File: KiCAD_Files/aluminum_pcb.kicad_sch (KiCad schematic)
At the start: 29 parts

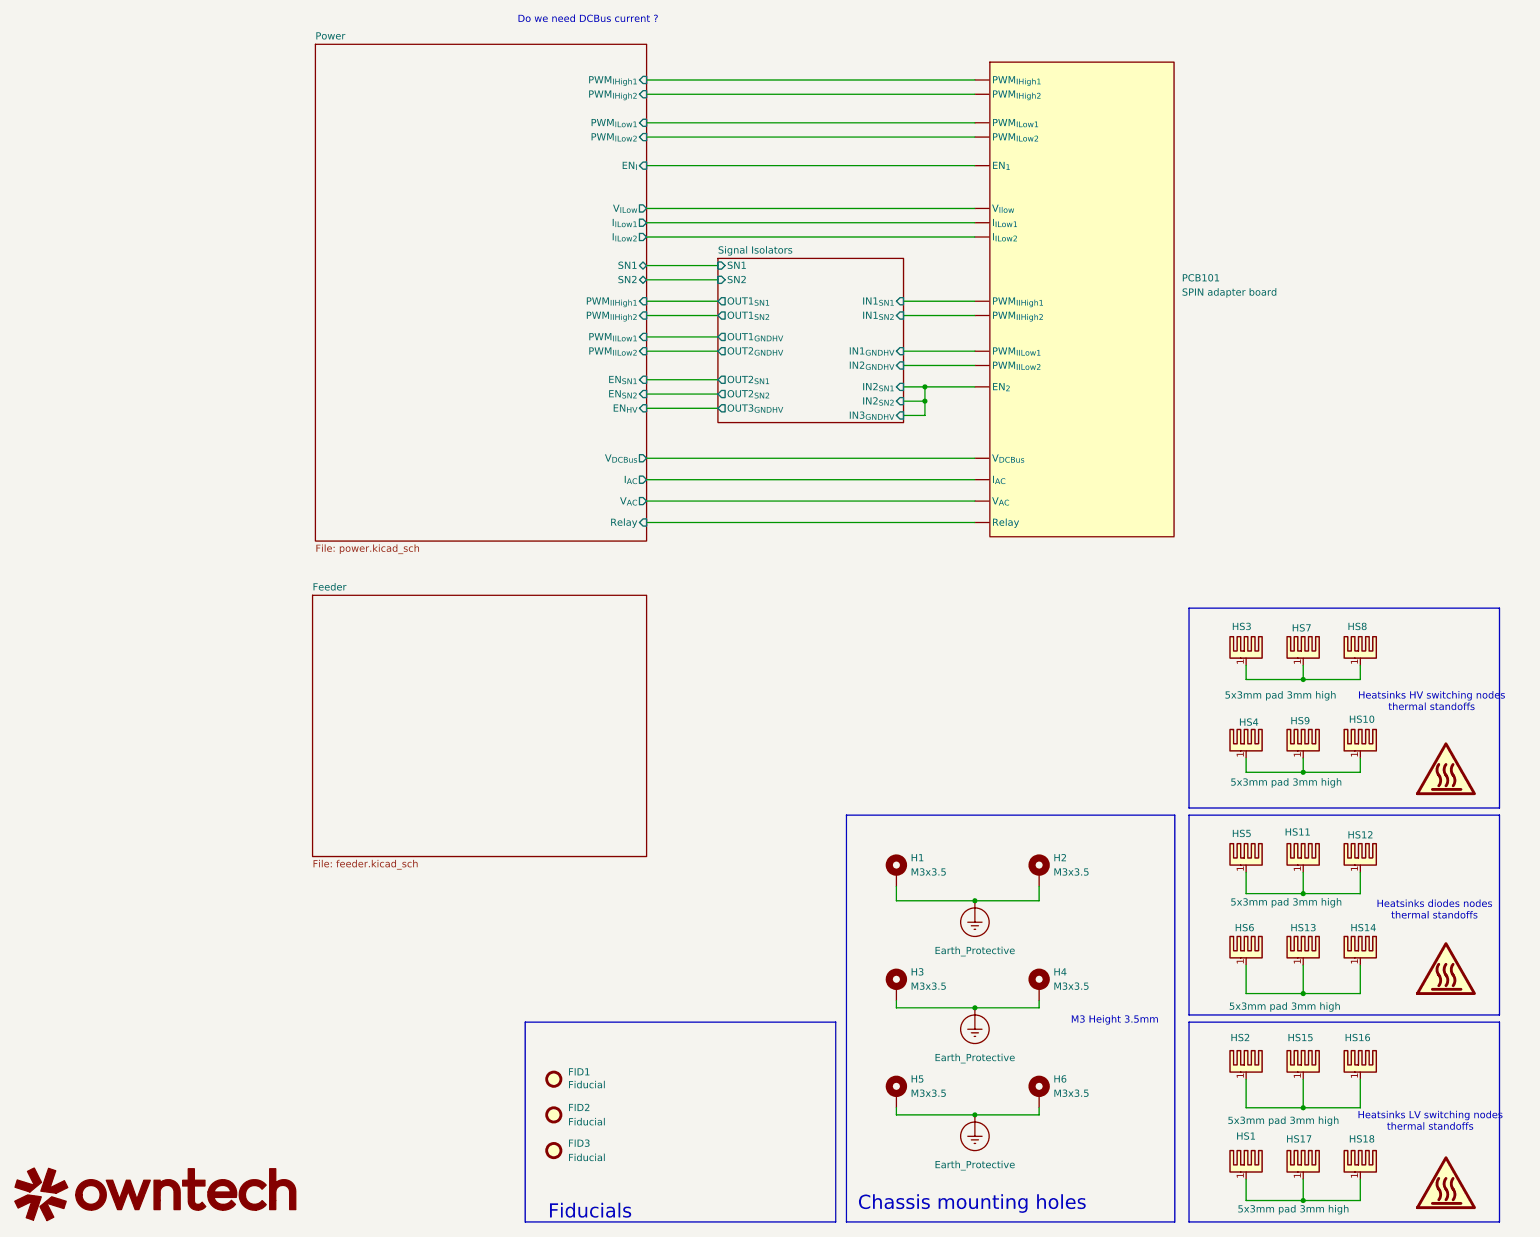
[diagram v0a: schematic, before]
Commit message: First routing pass complete.
Signed-off-by: Jean Alinei <jean.alinei@owntech.org>
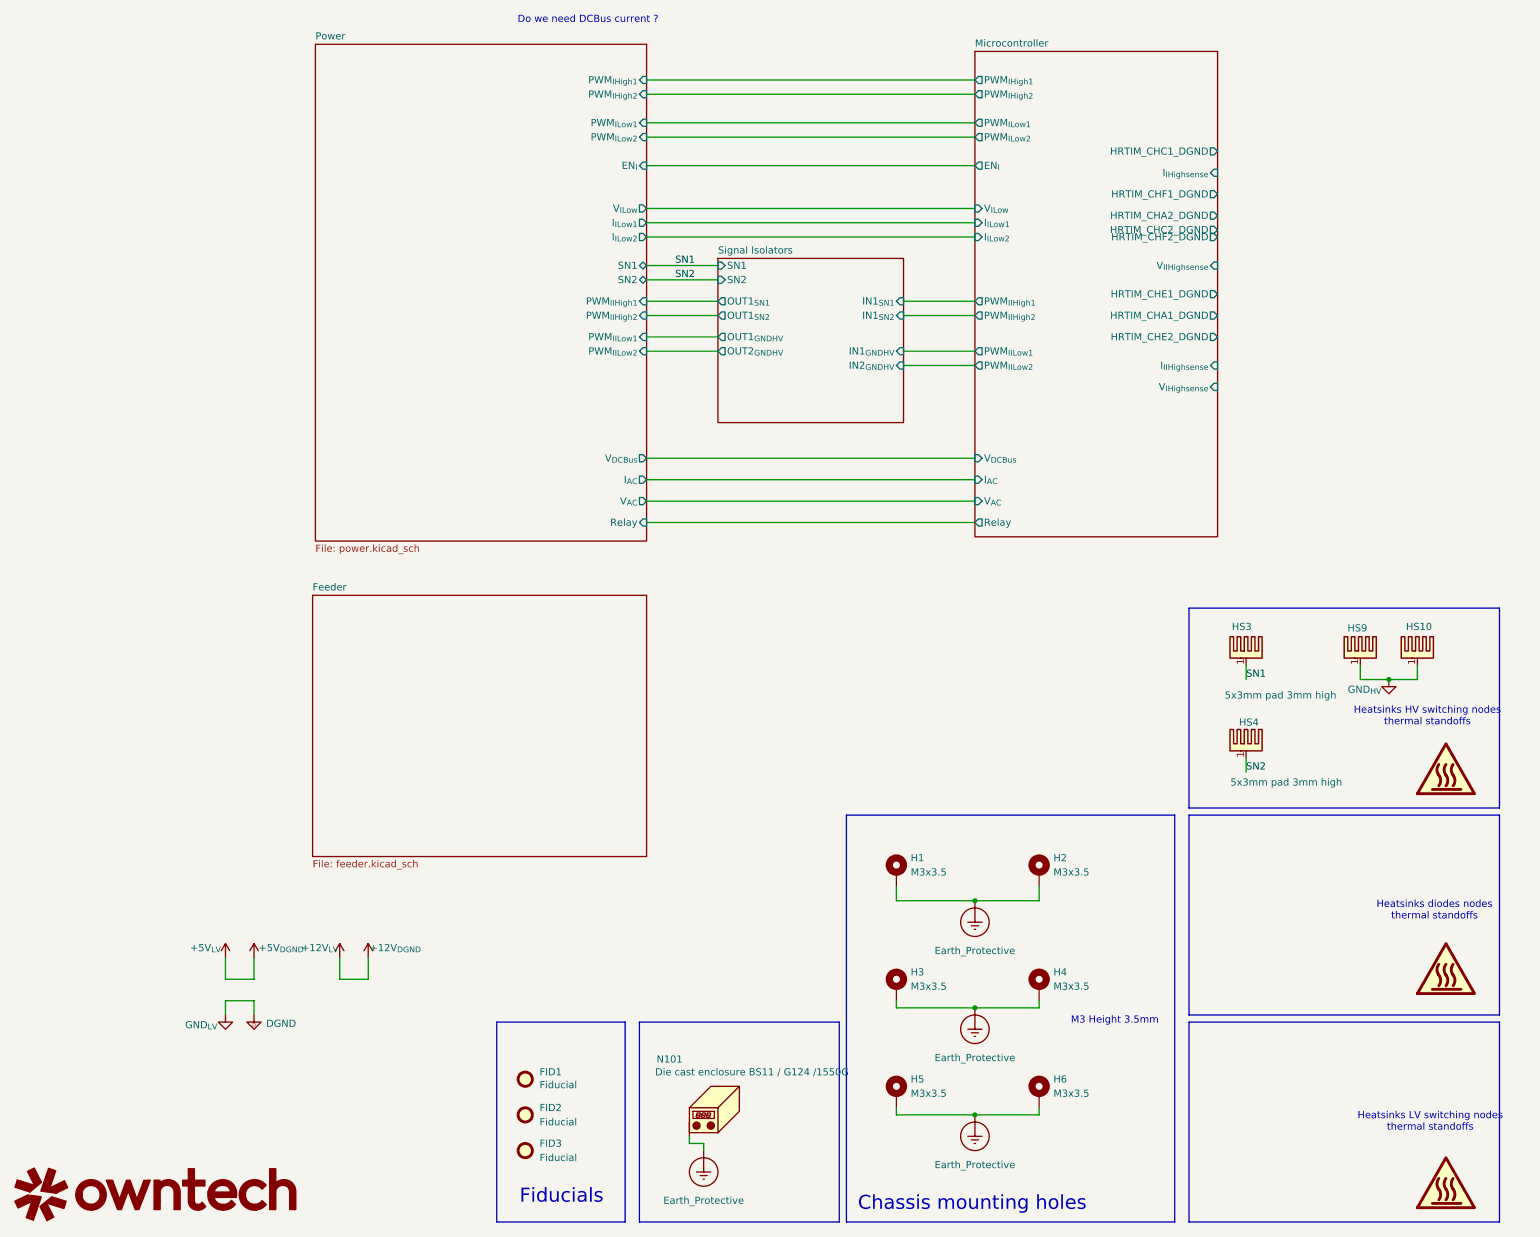
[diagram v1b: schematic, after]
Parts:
- removed HS1, HS11, HS12, HS13, HS14, HS15, HS16, HS17, HS18, HS2, HS5, HS6, HS7, HS8: 5x3mm pad 3mm high, Footprints:BTC-533-ZN01, symbol Mechanical:Heatsink_Pad
- removed PCB101: SPIN adapter board, symbol Symbols:SPIN_holder
- added N101: Die cast enclosure BS11 / G124 /1550G, Footprints:Die Cast Casing 1550G, symbol Mechanical:Housing_Pad
- Logo1: footprint (none) -> Footprints:owntech34mmneg
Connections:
- net Earth_Protective: now also N101.1 (PAD)
- net GND_{HV}: now reaches HS10.1, HS9.1
- net GND_{HV}: no longer HS4.1
- net SN1: now reaches HS3.1
- new net SN2: HS4.1
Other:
- added sheet Microcontroller (Microcontroller.kicad_sch)
- sheet Power ports: added none; removed EN_{HV}, EN_{SN1}, EN_{SN2}
- sheet Signal Isolators ports: added none; removed IN2_{SN1}, IN2_{SN2}, IN3_{GNDHV}, OUT2_{SN1}, OUT2_{SN2}, OUT3_{GNDHV}
- moved on the sheet: FID1, FID2, FID3, HS10, HS9

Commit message: Added missing tracks for sensors and relay. Fixed many routing issues.
Signed-off-by: Jean Alinei <jean.alinei@owntech.org>
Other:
- sheet Feeder ports: added DIS_{HV}, Neut_{REF}; removed none
- sheet Microcontroller ports: added DIS_{HV}; removed HRTIM_CHA1_DGND, HRTIM_CHA2_DGND, HRTIM_CHC1_DGND, HRTIM_CHC2_DGND, HRTIM_CHE1_DGND, HRTIM_CHE2_DGND, HRTIM_CHF1_DGND, HRTIM_CHF2_DGND, I_{IHighsense}, I_{IIHighsense}, V_{IHighsense}, V_{IIHighsense}
- sheet Power ports: added Neut_{REF}; removed none
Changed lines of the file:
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@@
+	(wire
+		(pts
+			(xy 201.93 160.02) (xy 201.93 175.26)
+		)
+		(stroke
+			(width 0)
+			(type default)
+		)
+	)
 	(wire
 		(pts
@@
 	(wire
 		(pts
+			(xy 201.93 175.26) (xy 128.27 175.26)
+		)
+		(stroke
+			(width 0)
+			(type default)
+		)
+	)
+	(wire
+		(pts
 			(xy 173.99 129.54) (xy 186.69 129.54)
 		)
@@
 		(pts
 			(xy 128.27 93.98) (xy 186.69 93.98)
+		)
+		(stroke
+			(width 0)
+			(type default)
+		)
+	)
+	(wire
+		(pts
+			(xy 102.87 161.29) (xy 102.87 170.18)
 		)
 		(stroke
@@
 	(sheet
 		(at 69.342 72.39)
-		(size 58.928 88.392)
+		(size 58.928 88.9)
 		(exclude_from_sim no)
 		(in_bom yes)
@@
 		)
 		(property "Sheetfile" "power.kicad_sch"
-			(at 69.342 161.3666 0)
+			(at 69.342 161.8746 0)
 			(effects
 				(font
@@
 				)
 				(justify right)
+			)
+		)
+		(pin "Neut_{REF}" output
+			(at 102.87 161.29 270)
+			(effects
+				(font
+					(size 1.27 1.27)
+				)
+				(justify left)
 			)
 		)
@@
 			)
 		)
-		(pin "HRTIM_CHC1_DGND" output
-			(at 229.87 91.44 0)
-			(effects
-				(font
-					(size 1.27 1.27)
-				)
-				(justify right)
-			)
-		)
 		(pin "I_{AC}" input
 			(at 186.69 149.86 180)
@@
 			)
 		)
-		(pin "I_{IHighsense}" input
-			(at 229.87 95.25 0)
-			(effects
-				(font
-					(size 1.27 1.27)
-				)
-				(justify right)
-			)
-		)
-		(pin "HRTIM_CHF1_DGND" output
-			(at 229.87 99.06 0)
-			(effects
-				(font
-					(size 1.27 1.27)
-				)
-				(justify right)
-			)
-		)
 		(pin "PWM_{ILow1}" output
 			(at 186.69 86.36 180)
@@
 			)
 		)
-		(pin "HRTIM_CHA2_DGND" output
-			(at 229.87 102.87 0)
-			(effects
-				(font
-					(size 1.27 1.27)
-				)
-				(justify right)
-			)
-		)
 		(pin "PWM_{IIHigh1}" output
 			(at 186.69 118.11 180)
@@
 			)
 		)
-		(pin "HRTIM_CHC2_DGND" output
-			(at 229.87 105.41 0)
-			(effects
-				(font
-					(size 1.27 1.27)
-				)
-				(justify right)
-			)
-		)
 		(pin "PWM_{IHigh1}" output
 			(at 186.69 78.74 180)
@@
 			)
 		)
-		(pin "HRTIM_CHF2_DGND" output
-			(at 229.87 106.68 0)
-			(effects
-				(font
-					(size 1.27 1.27)
-				)
-				(justify right)
-			)
-		)
 		(pin "PWM_{IILow2}" output
 			(at 186.69 129.54 180)
@@
 			)
 		)
-		(pin "V_{IIHighsense}" input
-			(at 229.87 111.76 0)
-			(effects
-				(font
-					(size 1.27 1.27)
-				)
-				(justify right)
-			)
-		)
-		(pin "HRTIM_CHE1_DGND" output
-			(at 229.87 116.84 0)
-			(effects
-				(font
-					(size 1.27 1.27)
-				)
-				(justify right)
-			)
-		)
-		(pin "HRTIM_CHA1_DGND" output
-			(at 229.87 120.65 0)
-			(effects
-				(font
-					(size 1.27 1.27)
-				)
-				(justify right)
-			)
-		)
 		(pin "I_{ILow2}" input
 			(at 186.69 106.68 180)
@@
 			)
 		)
-		(pin "HRTIM_CHE2_DGND" output
-			(at 229.87 124.46 0)
-			(effects
-				(font
-					(size 1.27 1.27)
-				)
-				(justify right)
-			)
-		)
 		(pin "PWM_{ILow2}" output
 			(at 186.69 88.9 180)
@@
 			)
 		)
-		(pin "I_{IIHighsense}" input
-			(at 229.87 129.54 0)
-			(effects
-				(font
-					(size 1.27 1.27)
-				)
-				(justify right)
-			)
-		)
 		(pin "PWM_{IIHigh2}" output
 			(at 186.69 120.65 180)
@@
 			)
 		)
-		(pin "V_{IHighsense}" input
-			(at 229.87 133.35 0)
-			(effects
-				(font
-					(size 1.27 1.27)
-				)
-				(justify right)
-			)
-		)
 		(pin "V_{DCBus}" input
 			(at 186.69 146.05 180)
@@
 			)
 		)
+		(pin "DIS_{HV}" output
+			(at 201.93 160.02 270)
+			(effects
+				(font
+					(size 1.27 1.27)
+				)
+				(justify left)
+			)
+		)
 		(instances
 			(project "aluminum_pcb"
@@
 	)
 	(sheet
-		(at 68.834 170.434)
-		(size 59.436 46.482)
+		(at 68.834 170.18)
+		(size 59.436 46.736)
 		(exclude_from_sim no)
 		(in_bom yes)
@@
 		)
 		(property "Sheetname" "Feeder"
-			(at 68.834 169.7224 0)
+			(at 68.834 169.4684 0)
 			(effects
 				(font
@@
 			)
 		)
+		(pin "DIS_{HV}" input
+			(at 128.27 175.26 0)
+			(effects
+				(font
+					(size 1.27 1.27)
+				)
+				(justify right)
+			)
+		)
+		(pin "Neut_{REF}" input
+			(at 102.87 170.18 90)
+			(effects
+				(font
+					(size 1.27 1.27)
+				)
+				(justify right)
+			)
+		)

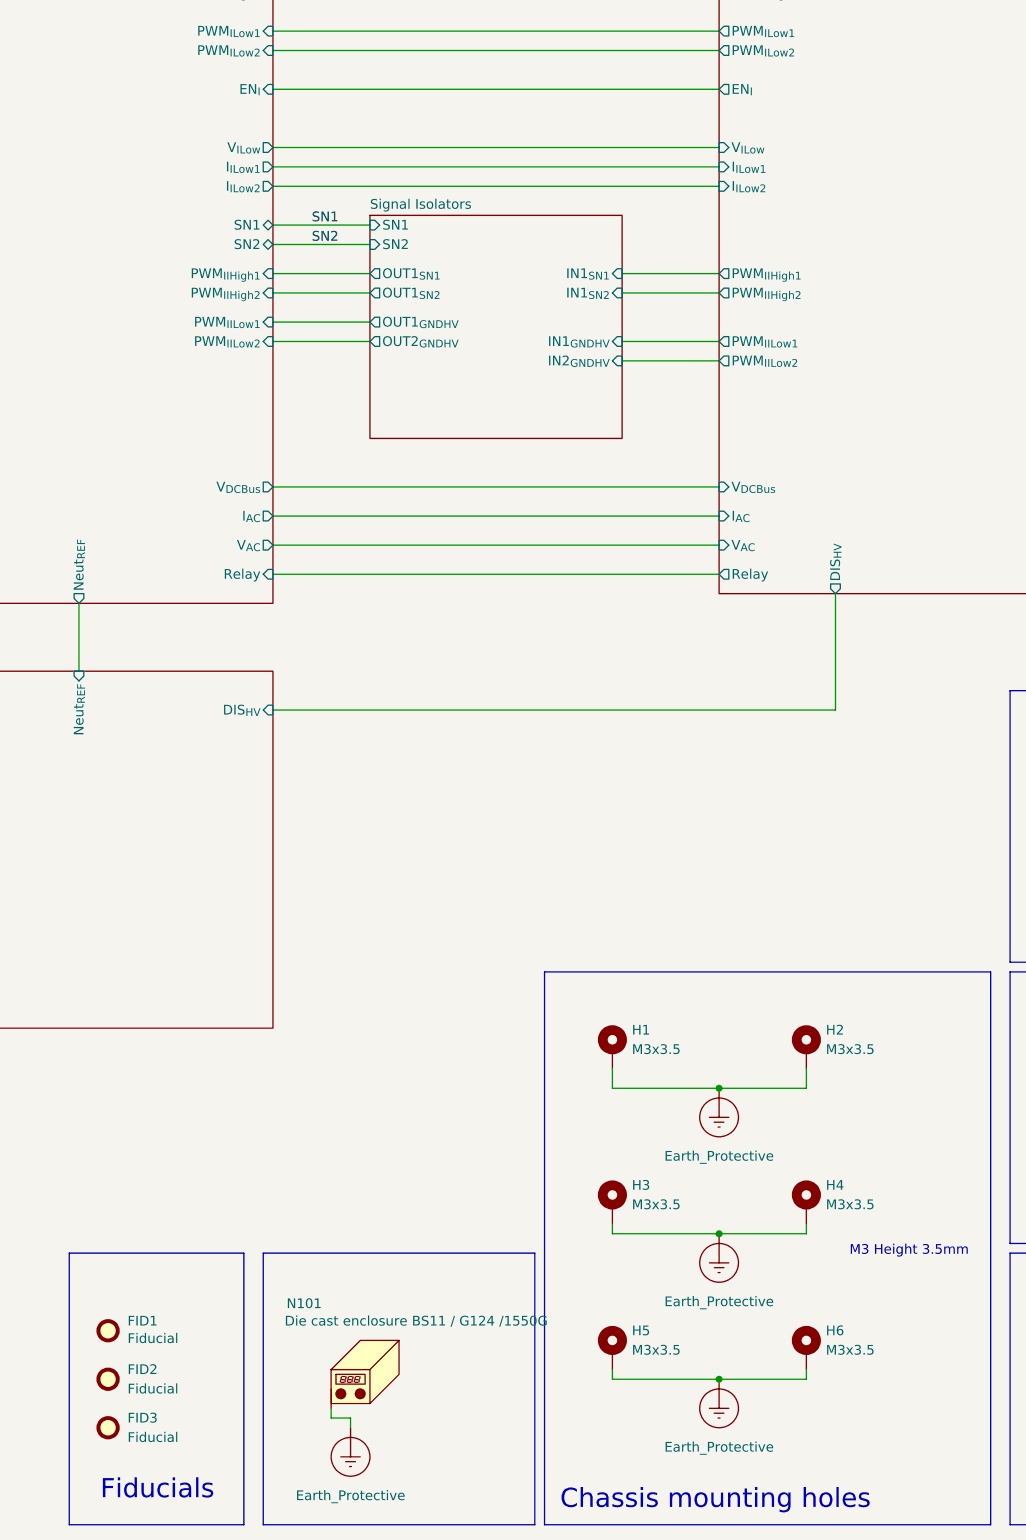
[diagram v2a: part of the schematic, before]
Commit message: Added DRC rules according to IEC60664 and IPC2221.
Signed-off-by: Jean Alinei <jean.alinei@owntech.org>
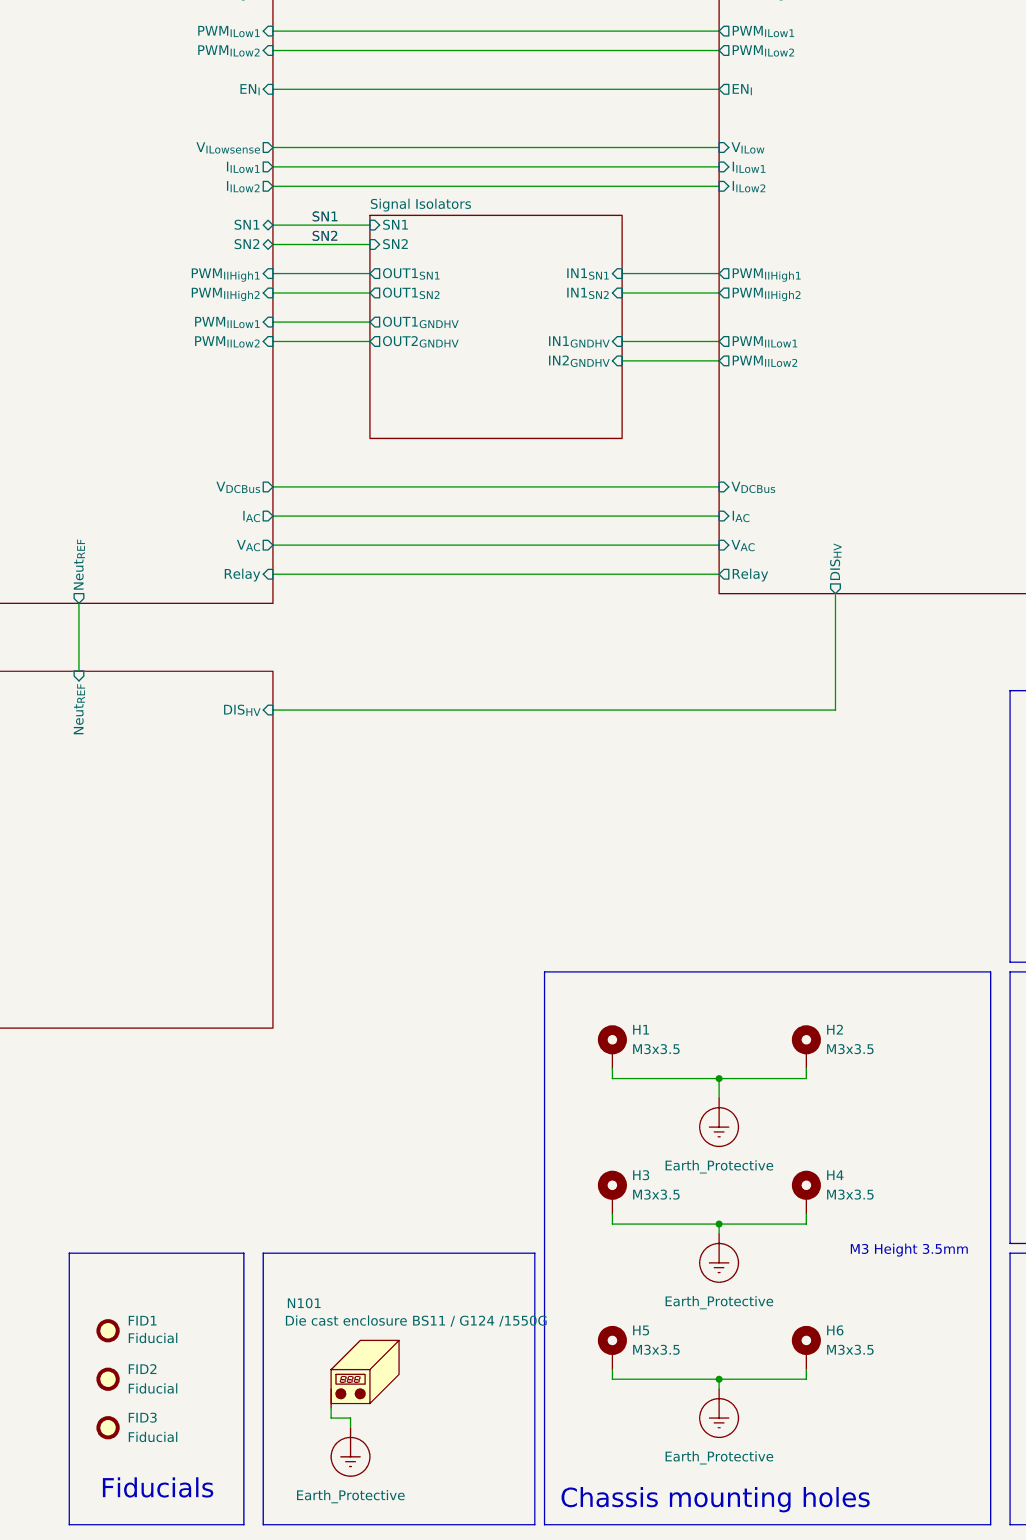
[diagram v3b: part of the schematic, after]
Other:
- sheet Power ports: added V_{ILowsense}; removed V_{ILow}
- moved on the sheet: H3, H4

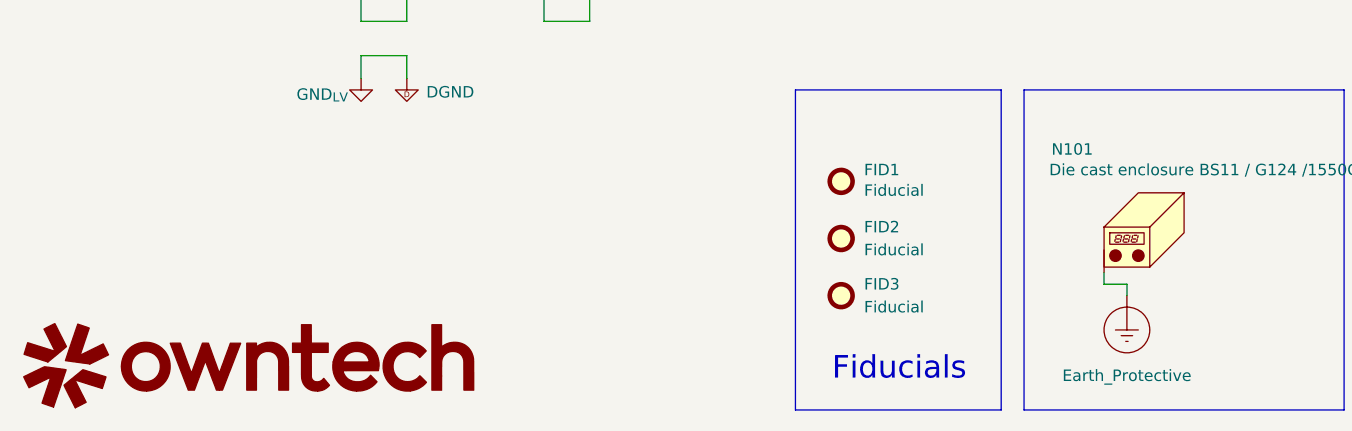
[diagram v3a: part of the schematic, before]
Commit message: Added passive references. Added ESD protection for MCU pins.
Signed-off-by: Jean Alinei <jean.alinei@owntech.org>
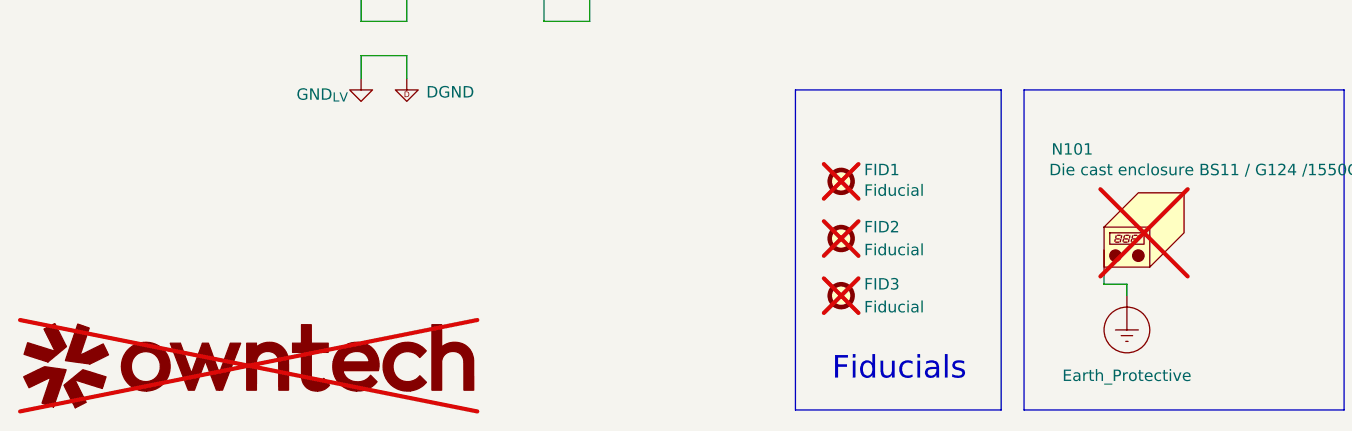
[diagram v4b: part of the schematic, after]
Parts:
- FID1, FID2, FID3, Logo1: now not fitted
- H1, H2, H3, H4, H5, H6: now in the parts list
- N101: now not fitted; now left out of the parts list
